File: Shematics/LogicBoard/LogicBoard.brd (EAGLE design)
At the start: 152.1 x 99 mm, 8 parts

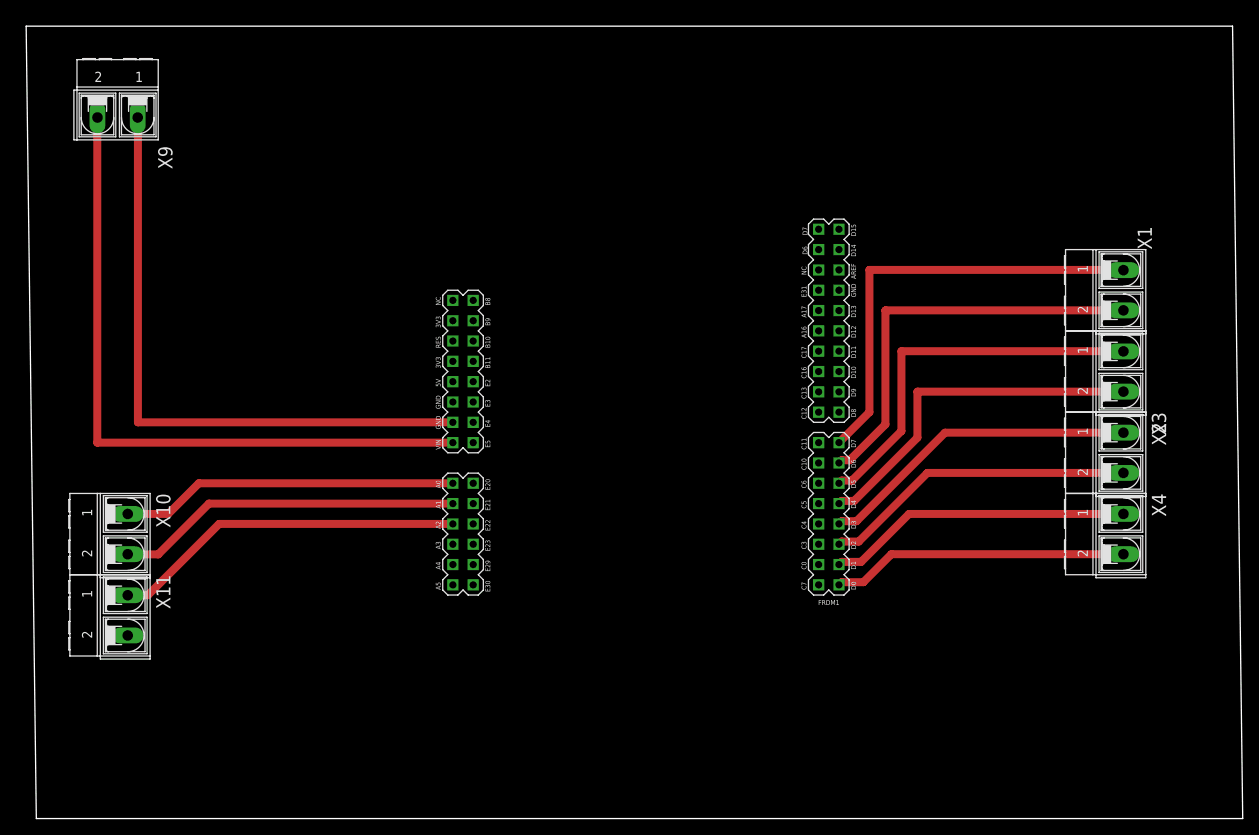
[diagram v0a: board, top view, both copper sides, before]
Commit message: Refactored logic board & completed power distribution board
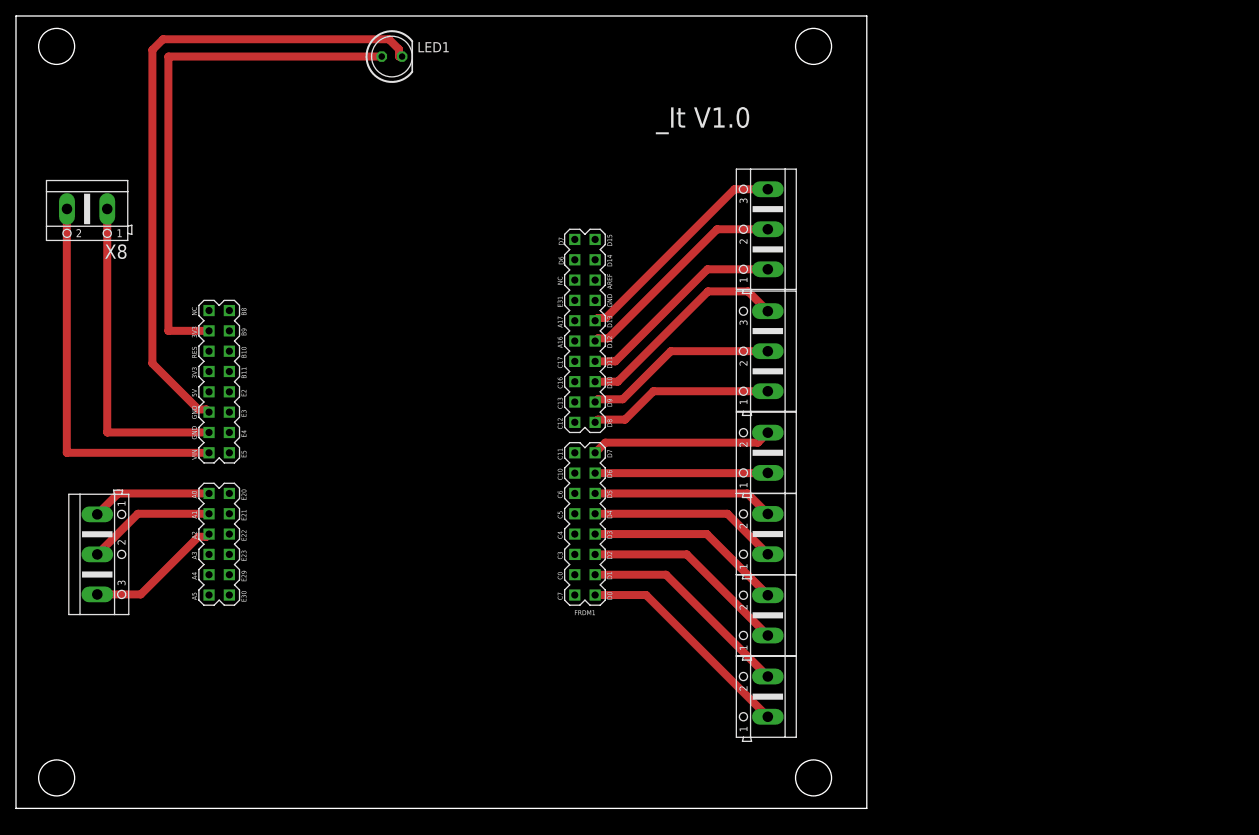
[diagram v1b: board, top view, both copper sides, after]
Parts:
- removed X10, X11, X9: (no value), con-ptr500:AK500/2-H
- added LED1: (no value), led:LED5MM
- added X5, X6, X7: (no value), con-ptr500:AK500/3
- added X8: (no value), con-ptr500:AK500/2
- X1, X2, X3, X4: device con-ptr500:AK500/2-H -> con-ptr500:AK500/2
- moved X1 48.9 mm to (94.0, 44.5), turned to 90 degrees
- moved X2 48.9 mm to (94.0, 34.3), turned to 90 degrees
- moved X3 48.9 mm to (94.0, 24.1), turned to 90 degrees
- moved X4 48.9 mm to (94.0, 14.0), turned to 90 degrees
- moved FRDM1 30.5 mm to (48.3, 44.5)
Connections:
- new net N$14: FRDM1.D8, X6.1
- new net N$15: FRDM1.D9, X6.2
- new net N$16: FRDM1.D10, X6.3
- new net N$17: FRDM1.D11, X7.1
- new net N$18: FRDM1.D12, X7.2
- new net N$19: FRDM1.D13, X7.3
- new net N$21: FRDM1.GND1, LED1.K
- new net N$22: FRDM1.3V3, LED1.A
- net N$1: now also X1.2; no longer X1.1
- net N$10: now also FRDM1.VIN, X8.2; no longer FRDM1.GND0, X9.1
- net N$11: now also X5.1; no longer X10.1
- net N$12: now also X5.2; no longer X10.2
- net N$13: now also X5.3; no longer X11.1
- net N$2: now also X1.1; no longer X1.2
- net N$3: now also X2.2; no longer X2.1
- net N$4: now also X2.1; no longer X2.2
- net N$5: now also X3.2; no longer X3.1
- net N$6: now also X3.1; no longer X3.2
- net N$7: now also X4.2; no longer X4.1
- net N$8: now also X4.1; no longer X4.2
- net N$9: now also FRDM1.GND0, X8.1; no longer FRDM1.VIN, X9.2
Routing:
- net N$21: track 0.00 -> 82.0 mm
- net N$22: track 0.00 -> 66.0 mm
- net N$9: track 85.1 -> 40.7 mm
- net N$1: track 54.9 -> 22.6 mm
- net N$2: track 51.8 -> 21.6 mm
- net N$10: track 77.5 -> 48.3 mm
- net N$19: track 0.00 -> 28.4 mm
- net N$18: track 0.00 -> 27.4 mm
- net N$16: track 0.00 -> 27.3 mm
- net N$13: track 44.3 -> 17.1 mm
- net N$12: track 43.3 -> 16.1 mm
- net N$11: track 42.2 -> 15.1 mm
- net N$17: track 0.00 -> 26.4 mm
- net N$3: track 48.2 -> 22.7 mm
- net N$15: track 0.00 -> 24.2 mm
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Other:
- board size 152.1 x 99 mm -> 106.3 x 99 mm
- board text added: "_It V1.0"
